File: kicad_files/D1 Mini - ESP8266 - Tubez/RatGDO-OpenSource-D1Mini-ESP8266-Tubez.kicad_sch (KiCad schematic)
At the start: 23 parts, among them J1 Screw_Terminal_01x03, J2 Conn_01x11, J3 Screw_Terminal_01x02, Q1 2N7002, Q2 AO3400A, Q3 AO3400A, Q4 AO3400A, U1 WeMos_D1_mini, U2 K7805-500R3

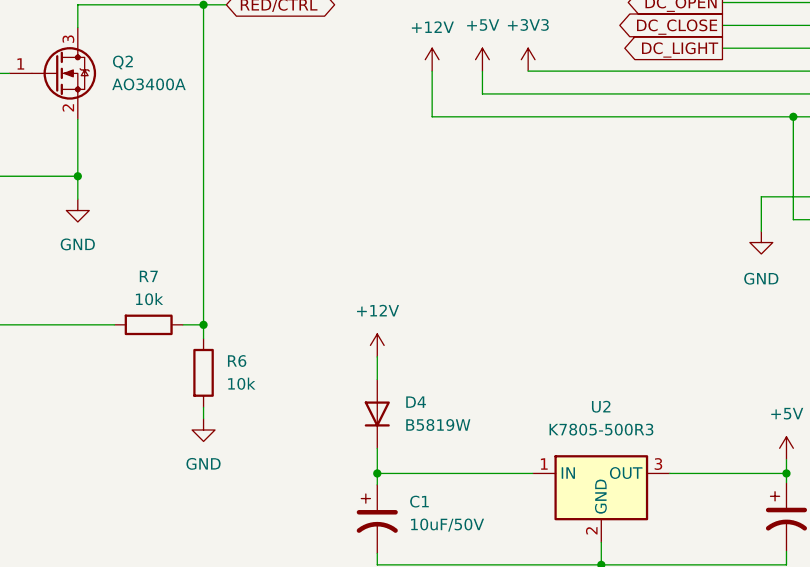
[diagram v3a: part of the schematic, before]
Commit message: Added 500mA fuse to input power
fuse is expensive on jlcpcb.  need to explore other part numbers., maybe move to 1206 size ptc instead.
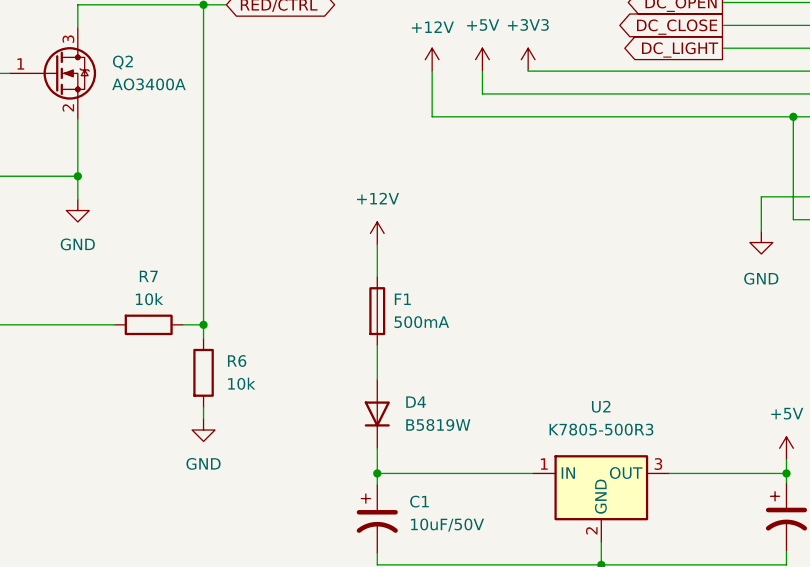
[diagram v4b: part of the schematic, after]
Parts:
- added F1: 500mA, Fuse:Fuse_0805_2012Metric_Pad1.15x1.40mm_HandSolder, symbol Device:Fuse
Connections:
- net +12V: now also F1.1; no longer D4.2 (A)
- new net: D4.2 (A), F1.2
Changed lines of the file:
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@@
-    (stroke (width 0) (type default))
-  )
-  (wire (pts (xy 172.212 125.476) (xy 172.212 128.016))
     (stroke (width 0) (type default))
   )
@@
     (stroke (width 0) (type default))
   )
+  (wire (pts (xy 172.212 113.03) (xy 172.212 116.586))
+    (stroke (width 0) (type default))
+  )
   (wire (pts (xy 80.01 139.7) (xy 82.55 139.7))
     (stroke (width 0) (type default))
@@
   )
   (wire (pts (xy 138.938 86.36) (xy 152.908 86.36))
+    (stroke (width 0) (type default))
+  )
+  (wire (pts (xy 172.212 124.206) (xy 172.212 128.016))
     (stroke (width 0) (type default))
   )
@@
         (path "/d526daf5-1a87-4c4a-b8db-6120ccadc008"
           (reference "#PWR06") (unit 1)
+        )
+      )
+    )
+  )
+  (symbol (lib_id "Device:Fuse") (at 172.212 120.396 0) (unit 1)
+    (in_bom yes) (on_board yes) (dnp no) (fields_autoplaced)
+    (property "Reference" "F1" (at 173.99 119.126 0)
+      (effects (font (size 1.27 1.27)) (justify left))
+    )
+    (property "Value" "500mA" (at 173.99 121.666 0)
+      (effects (font (size 1.27 1.27)) (justify left))
+    )
+    (property "Footprint" "Fuse:Fuse_0805_2012Metric_Pad1.15x1.40mm_HandSolder" (at 170.434 120.396 90)
+      (effects (font (size 1.27 1.27)) hide)
+    )
+    (property "Datasheet" "~" (at 172.212 120.396 0)
+      (effects (font (size 1.27 1.27)) hide)
+    )
+    (pin "1")
+    (pin "2")
+    (instances
+      (project "RatGDO-OpenSource-D1Mini-ESP8266-Tubez"
+        (path "/d526daf5-1a87-4c4a-b8db-6120ccadc008"
+          (reference "F1") (unit 1)
         )
       )
@@
     )
   )
-  (symbol (lib_id "power:+12V") (at 172.212 125.476 0) (unit 1)
-    (in_bom yes) (on_board yes) (dnp no) (fields_autoplaced)
-    (property "Reference" "#PWR013" (at 172.212 129.286 0)
-      (effects (font (size 1.27 1.27)) hide)
-    )
-    (property "Value" "+12V" (at 172.212 120.396 0)
-      (effects (font (size 1.27 1.27)))
-    )
-    (property "Footprint" "" (at 172.212 125.476 0)
-      (effects (font (size 1.27 1.27)) hide)
-    )
-    (property "Datasheet" "" (at 172.212 125.476 0)
-      (effects (font (size 1.27 1.27)) hide)
-    )
+  (symbol (lib_id "power:+12V") (at 172.212 113.03 0) (unit 1)
+    (in_bom yes) (on_board yes) (dnp no) (fields_autoplaced)
+    (property "Reference" "#PWR013" (at 172.212 116.84 0)
+      (effects (font (size 1.27 1.27)) hide)
+    )
+    (property "Value" "+12V" (at 172.212 107.95 0)
+      (effects (font (size 1.27 1.27)))
+    )
+    (property "Footprint" "" (at 172.212 113.03 0)
+      (effects (font (size 1.27 1.27)) hide)
+    )
+    (property "Datasheet" "" (at 172.212 113.03 0)
+      (effects (font (size 1.27 1.27)) hide)
+    )

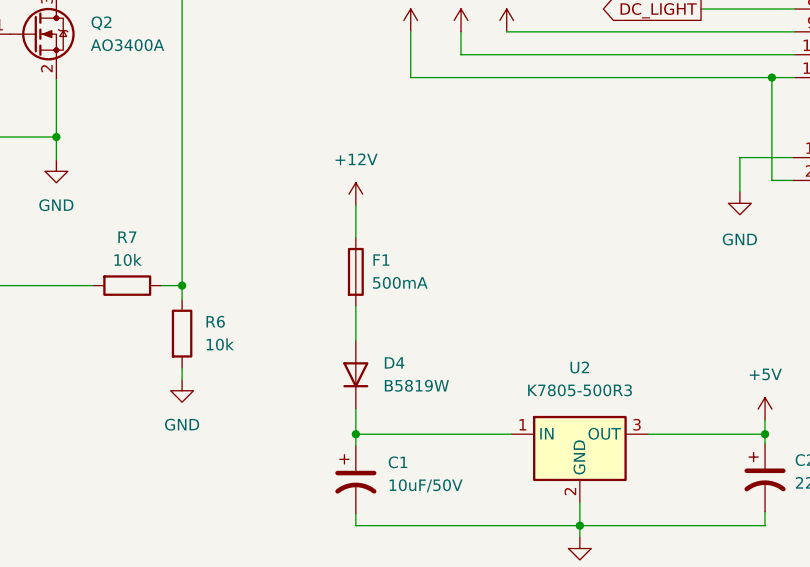
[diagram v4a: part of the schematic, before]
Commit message: Change to 750mA fuse 1206 package
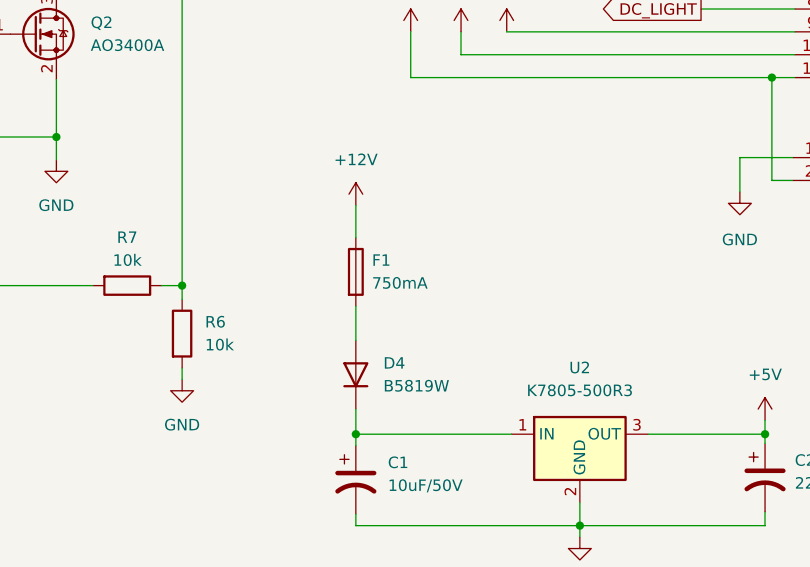
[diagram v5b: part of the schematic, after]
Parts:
- F1: value 500mA -> 750mA; footprint Fuse:Fuse_0805_2012Metric_Pad1.15x1.40mm_HandSolder -> Fuse:Fuse_1206_3216Metric_Pad1.42x1.75mm_HandSolder
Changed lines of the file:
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@@
       (effects (font (size 1.27 1.27)) (justify left))
     )
-    (property "Value" "500mA" (at 173.99 121.666 0)
+    (property "Value" "750mA" (at 173.99 121.666 0)
       (effects (font (size 1.27 1.27)) (justify left))
     )
-    (property "Footprint" "Fuse:Fuse_0805_2012Metric_Pad1.15x1.40mm_HandSolder" (at 170.434 120.396 90)
+    (property "Footprint" "Fuse:Fuse_1206_3216Metric_Pad1.42x1.75mm_HandSolder" (at 170.434 120.396 90)
       (effects (font (size 1.27 1.27)) hide)
     )

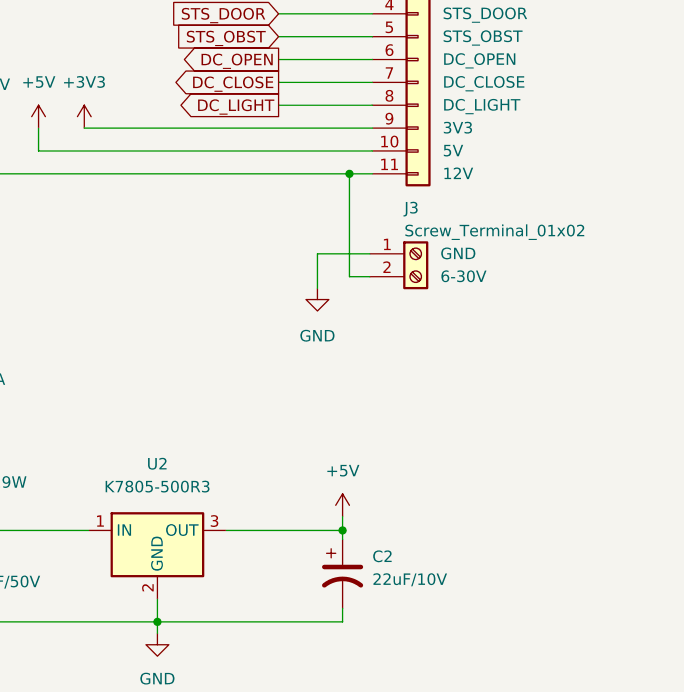
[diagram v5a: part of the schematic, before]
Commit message: Add 3v3 or 5V jumper for use of different dcdc
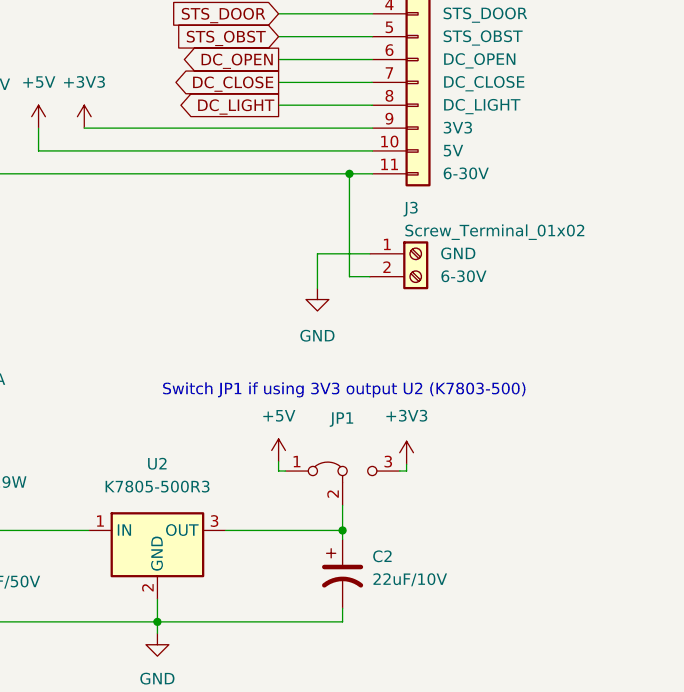
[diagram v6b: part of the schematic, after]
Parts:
- added JP1: ~, Custom Library:SolderJumper-3_P1.3mm_Bridged2Bar12_RoundedPad1.0x1.5mm_voltjump, symbol Jumper:Jumper_3_Bridged12
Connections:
- net +3V3: now also JP1.3 (B)
- net +5V: now also JP1.1 (A); no longer C2.1, U2.3 (OUT)
- new net: C2.1, JP1.2 (C), U2.3 (OUT)
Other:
- note added: "Switch JP1 if using 3V3 output U2 (K7803-500)"
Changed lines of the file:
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@@
   (junction (at 120.904 93.98) (diameter 0) (color 0 0 0 0)
   )
+  (junction (at 217.678 138.43) (diameter 0) (color 0 0 0 0)
+  )
   (junction (at 213.106 53.086) (diameter 0) (color 0 0 0 0)
   )
   (junction (at 218.44 98.806) (diameter 0) (color 0 0 0 0)
-  )
-  (junction (at 217.678 138.43) (diameter 0) (color 0 0 0 0)
   )
   (junction (at 197.104 148.59) (diameter 0) (color 0 0 0 0)
@@
     (stroke (width 0) (type default))
   )
+  (wire (pts (xy 210.566 130.81) (xy 210.566 131.826))
+    (stroke (width 0) (type default))
+  )
   (wire (pts (xy 218.44 98.806) (xy 178.308 98.806))
     (stroke (width 0) (type default))
@@
     (stroke (width 0) (type default))
   )
+  (wire (pts (xy 224.79 131.064) (xy 224.79 131.826))
+    (stroke (width 0) (type default))
+  )
   (wire (pts (xy 120.396 53.34) (xy 121.92 53.34))
     (stroke (width 0) (type default))
@@
     (stroke (width 0) (type default))
   )
+  (wire (pts (xy 217.678 135.636) (xy 217.678 138.43))
+    (stroke (width 0) (type default))
+  )
   (wire (pts (xy 120.904 105.41) (xy 138.938 105.41))
     (stroke (width 0) (type default))
@@
     (stroke (width 0) (type default))
   )
+  (wire (pts (xy 204.724 138.43) (xy 217.678 138.43))
+    (stroke (width 0) (type default))
+  )
   (wire (pts (xy 220.726 110.236) (xy 218.44 110.236))
     (stroke (width 0) (type default))
@@
     (stroke (width 0) (type default))
   )
-  (wire (pts (xy 217.678 136.906) (xy 217.678 138.43))
-    (stroke (width 0) (type default))
-  )
-  (wire (pts (xy 204.724 138.43) (xy 217.678 138.43))
-    (stroke (width 0) (type default))
-  )
   (wire (pts (xy 220.726 48.006) (xy 218.186 48.006))
     (stroke (width 0) (type default))
@@
     (stroke (width 0) (type default))
   )
+  (wire (pts (xy 211.328 131.826) (xy 210.566 131.826))
+    (stroke (width 0) (type default))
+  )
   (wire (pts (xy 59.69 91.44) (xy 59.69 53.34))
     (stroke (width 0) (type default))
@@
     (stroke (width 0) (type default))
   )
+  (wire (pts (xy 224.79 131.826) (xy 224.028 131.826))
+    (stroke (width 0) (type default))
+  )
   (wire (pts (xy 86.36 119.38) (xy 86.36 120.65))
     (stroke (width 0) (type default))
@@
   (wire (pts (xy 86.36 109.22) (xy 86.36 111.76))
     (stroke (width 0) (type default))
+  )
+  (text "Switch JP1 if using 3V3 output U2 (K7803-500)" (at 197.612 123.698 0)
+    (effects (font (size 1.27 1.27)) (justify left bottom))
   )
   (text "  id_prefix: ratgdov25\n  friendly_name: \"RATGDOv2.5\"\n  uart_tx_pin: D1\n  uart_rx_pin: D2\n  input_obst_pin: D7\n  status_door_pin: D0\n  status_obstruction_pin: D8\n  dry_contact_open_pin: D5\n  dry_contact_close_pin: D6\n  dry_contact_light_pin: D3"
@@
     )
   )
+  (symbol (lib_id "Jumper:Jumper_3_Bridged12") (at 217.678 131.826 0) (unit 1)
+    (in_bom yes) (on_board yes) (dnp no) (fields_autoplaced)
+    (property "Reference" "JP1" (at 217.678 125.984 0)
+      (effects (font (size 1.27 1.27)))
+    )
+    (property "Value" "~" (at 217.678 128.524 0)
+      (effects (font (size 1.27 1.27)))
+    )
+    (property "Footprint" "Custom Library:SolderJumper-3_P1.3mm_Bridged2Bar12_RoundedPad1.0x1.5mm_voltjump" (at 217.678 131.826 0)
+      (effects (font (size 1.27 1.27)) hide)
+    )
+    (property "Datasheet" "~" (at 217.678 131.826 0)
+      (effects (font (size 1.27 1.27)) hide)
+    )
+    (pin "1")
+    (pin "2")
+    (pin "3")
+    (instances
+      (project "RatGDO-OpenSource-D1Mini-ESP8266-Tubez"
+        (path "/d526daf5-1a87-4c4a-b8db-6120ccadc008"
+          (reference "JP1") (unit 1)
+        )
+      )
+    )
+  )
   (symbol (lib_id "Device:R") (at 86.36 115.57 0) (unit 1)
     (in_bom yes) (on_board yes) (dnp no) (fields_autoplaced)
@@
         (path "/d526daf5-1a87-4c4a-b8db-6120ccadc008"
           (reference "D1") (unit 1)
+        )
+      )
+    )
+  )
+  (symbol (lib_id "power:+3V3") (at 224.79 131.064 0) (unit 1)
+    (in_bom yes) (on_board yes) (dnp no) (fields_autoplaced)
+    (property "Reference" "#PWR018" (at 224.79 134.874 0)
+      (effects (font (size 1.27 1.27)) hide)
+    )
+    (property "Value" "+3V3" (at 224.79 125.73 0)
+      (effects (font (size 1.27 1.27)))
+    )
+    (property "Footprint" "" (at 224.79 131.064 0)
+      (effects (font (size 1.27 1.27)) hide)
+    )
+    (property "Datasheet" "" (at 224.79 131.064 0)
+      (effects (font (size 1.27 1.27)) hide)
+    )
+    (pin "1")
+    (instances
+      (project "RatGDO-OpenSource-D1Mini-ESP8266-Tubez"
+        (path "/d526daf5-1a87-4c4a-b8db-6120ccadc008"
+          (reference "#PWR018") (unit 1)
         )
       )
@@
     )
   )
-  (symbol (lib_id "power:+5V") (at 217.678 136.906 0) (unit 1)
-    (in_bom yes) (on_board yes) (dnp no) (fields_autoplaced)
-    (property "Reference" "#PWR014" (at 217.678 140.716 0)
-      (effects (font (size 1.27 1.27)) hide)
-    )
-    (property "Value" "+5V" (at 217.678 131.826 0)
-      (effects (font (size 1.27 1.27)))
-    )
-    (property "Footprint" "" (at 217.678 136.906 0)
-      (effects (font (size 1.27 1.27)) hide)
-    )
-    (property "Datasheet" "" (at 217.678 136.906 0)
-      (effects (font (size 1.27 1.27)) hide)
-    )
+  (symbol (lib_id "power:+5V") (at 210.566 130.81 0) (unit 1)
+    (in_bom yes) (on_board yes) (dnp no) (fields_autoplaced)
+    (property "Reference" "#PWR014" (at 210.566 134.62 0)
+      (effects (font (size 1.27 1.27)) hide)
+    )
+    (property "Value" "+5V" (at 210.566 125.73 0)
+      (effects (font (size 1.27 1.27)))
+    )
+    (property "Footprint" "" (at 210.566 130.81 0)
+      (effects (font (size 1.27 1.27)) hide)
+    )
+    (property "Datasheet" "" (at 210.566 130.81 0)
+      (effects (font (size 1.27 1.27)) hide)
+    )
